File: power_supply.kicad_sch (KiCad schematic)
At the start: 19 parts, among them J1 12V_DC, U121 TPS54560_A, U122 TPS54560_B

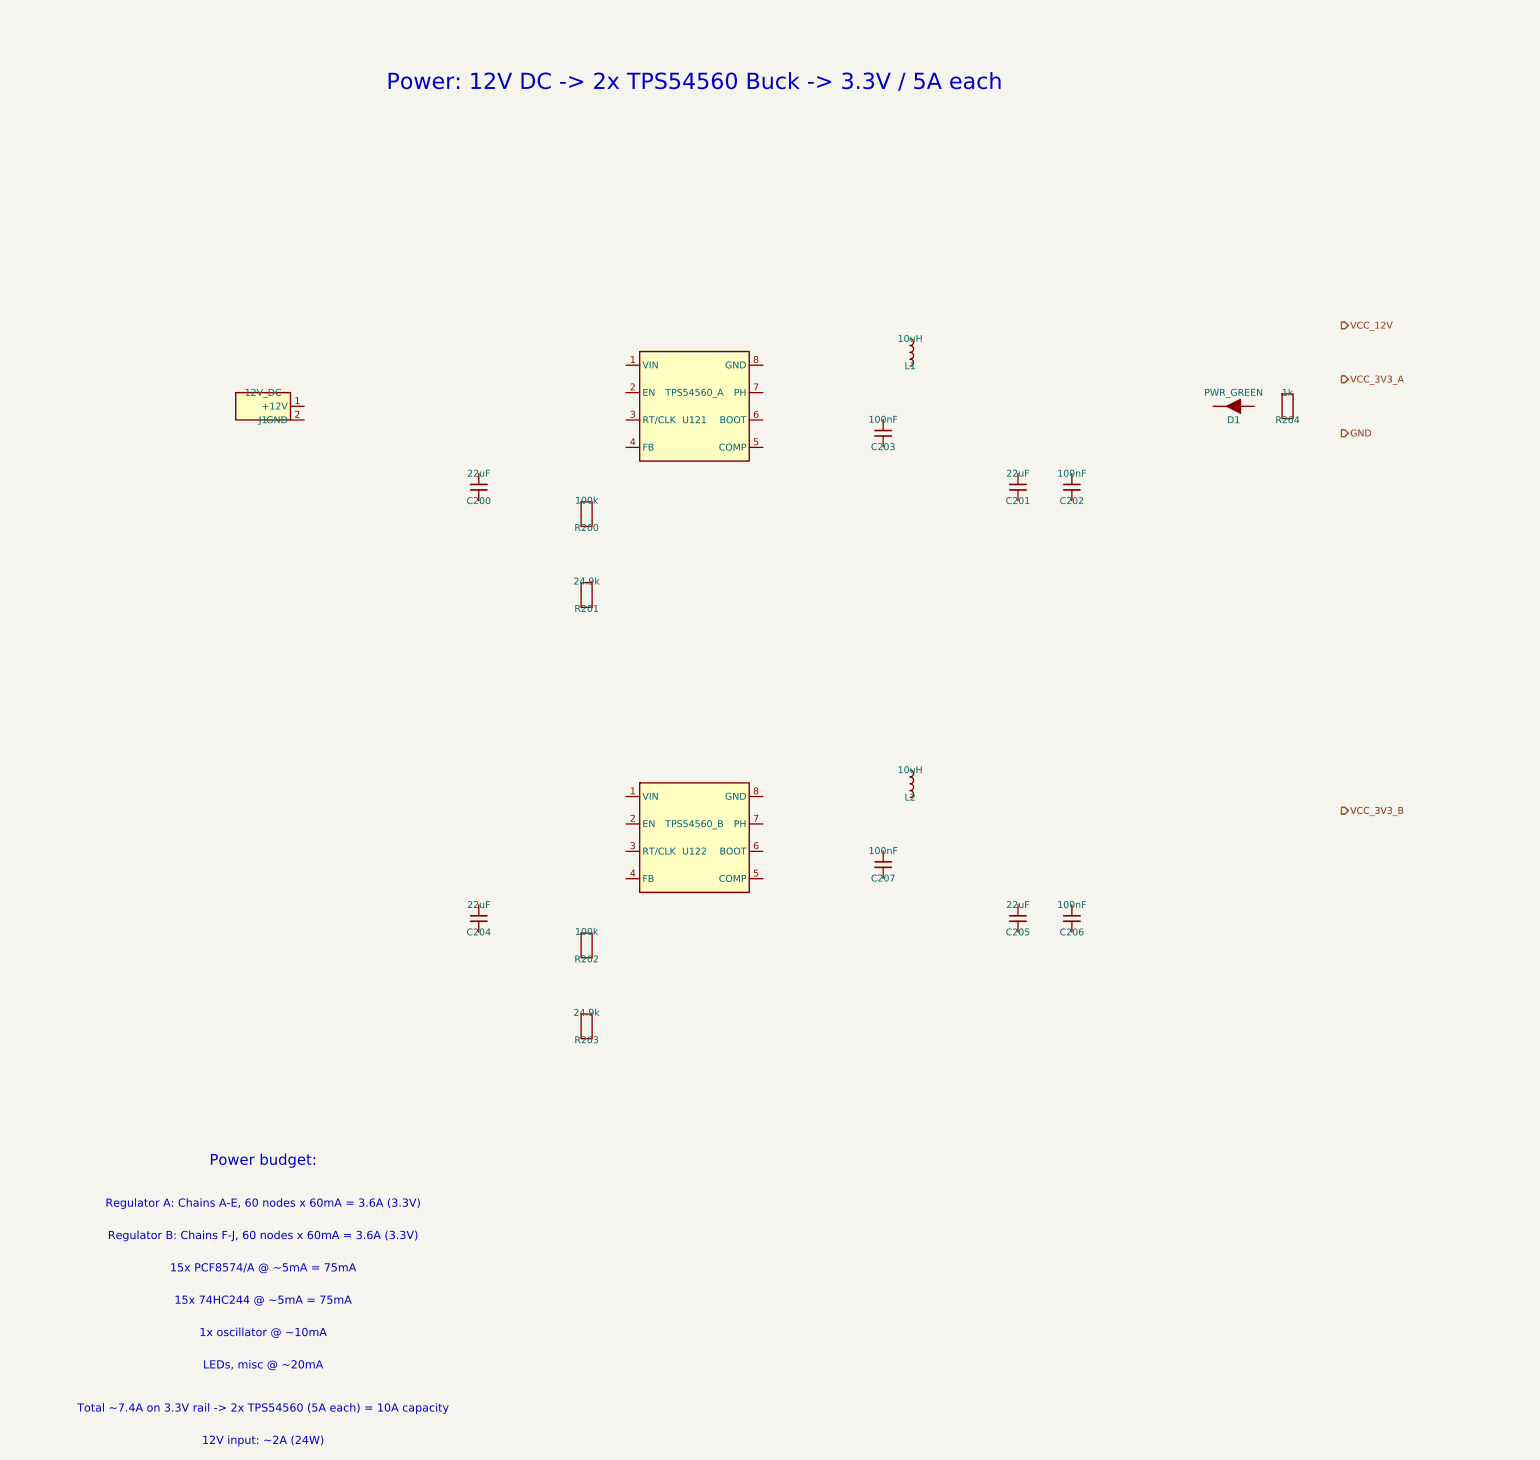
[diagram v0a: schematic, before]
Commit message: Regenerate KiCad output files for v1.0 architecture
Co-authored-by: Copilot <223556219+Copilot@users.noreply.github.com>
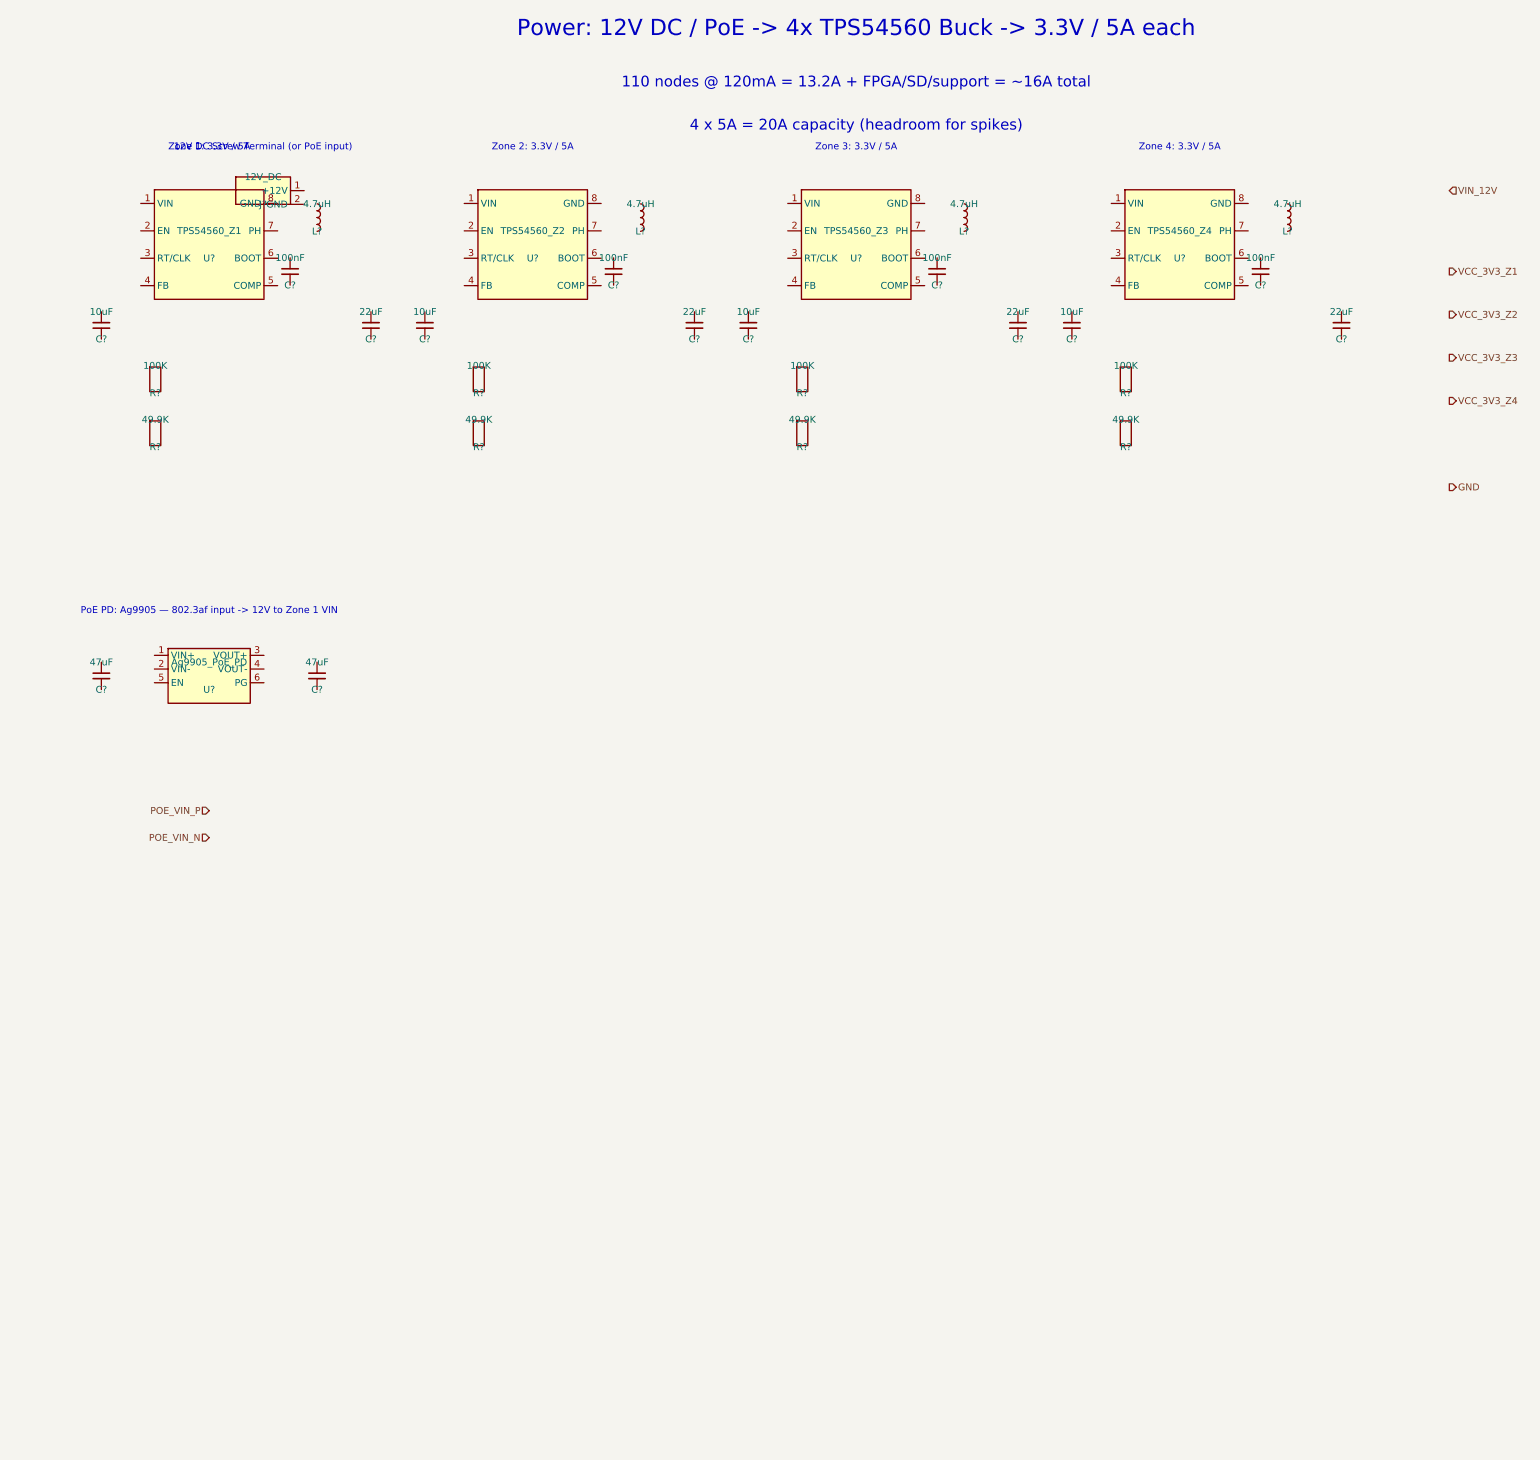
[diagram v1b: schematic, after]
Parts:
- removed C200, C201, C204, C205: 22uF, symbol Device:C
- removed C202, C203, C206, C207: 100nF, symbol Device:C
- removed D1: PWR_GREEN, symbol Device:LED
- removed J1: 12V_DC, symbol Connector:Barrel_Jack
- removed L1, L2: 10uH, symbol Device:L
- removed R200, R202: 100k, symbol Device:R
- removed R201, R203: 24.9k, symbol Device:R
- removed R204: 1k, symbol Device:R
- removed U121: TPS54560_A, symbol Regulator_Switching:TPS54560
- removed U122: TPS54560_B, symbol Regulator_Switching:TPS54560
- added C? (x4): 10uF, symbol Device:C
- added C? (x4): 22uF, symbol Device:C
- added C? (x4): 100nF, symbol Device:C
- added C? (x2): 47uF, symbol Device:C
- added J?: 12V_DC, symbol Connector:Screw_Terminal_01x02
- added L? (x4): 4.7uH, symbol Device:L
- added R? (x4): 100K, symbol Device:R
- added R? (x4): 49.9K, symbol Device:R
- added U?: TPS54560_Z1, symbol Regulator_Switching:TPS54560
- added U?: TPS54560_Z2, symbol Regulator_Switching:TPS54560
- added U?: TPS54560_Z3, symbol Regulator_Switching:TPS54560
- added U?: TPS54560_Z4, symbol Regulator_Switching:TPS54560
- added U?: Ag9905_PoE_PD, symbol Power_Management:Ag9905
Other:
- note added: "110 nodes @ 120mA = 13.2A + FPGA/SD/support = ~16A total"
- note added: "12V DC Screw Terminal (or PoE input)"
- note added: "4 x 5A = 20A capacity (headroom for spikes)"
- note added: "PoE PD: Ag9905 — 802.3af input -> 12V to Zone 1 VIN"
- note added: "Power: 12V DC / PoE -> 4x TPS54560 Buck -> 3.3V / 5A each"
- note added: "Zone 1: 3.3V / 5A"
- note added: "Zone 2: 3.3V / 5A"
- note added: "Zone 3: 3.3V / 5A"
- note added: "Zone 4: 3.3V / 5A"
- note removed: "12V input: ~2A (24W)"
- note removed: "15x 74HC244 @ ~5mA = 75mA"
- note removed: "15x PCF8574/A @ ~5mA = 75mA"
- note removed: "1x oscillator @ ~10mA"
- note removed: "LEDs, misc @ ~20mA"
- note removed: "Power budget:"
- note removed: "Power: 12V DC -> 2x TPS54560 Buck -> 3.3V / 5A each"
- note removed: "Regulator A: Chains A-E, 60 nodes x 60mA = 3.6A (3.3V)"
- note removed: "Regulator B: Chains F-J, 60 nodes x 60mA = 3.6A (3.3V)"
- note removed: "Total ~7.4A on 3.3V rail -> 2x TPS54560 (5A each) = 10A capacity"
- title: Power Supply — Dual TPS54560 12V to 3.3V -> Power Supply — 4-Zone + PoE PD
